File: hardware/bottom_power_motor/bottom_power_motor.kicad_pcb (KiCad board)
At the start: 4 copper layers, 52 x 52 mm, 82 parts, among them J1 Feld 16p, J2 J_STK_A, J3 J_STK_B, Q1 P-FET 40V 30A, U2 TPS54360, U2_CB 100n, U2_CO 47u, U2_CZ 3n3, U2_D 60V 3A, U2_L 10u, U2_RC 10k, U2_RH 53k6, U2_RL 10k2, U2_RT_R 100k, U3 TLV62569, U4 TPS54360, U4_CB 100n, U4_CO 22u, U4_CZ 3n3, U4_D 60V 3A, U4_L 33u, U4_RC 10k, U4_RH 68k1, U4_RL 10k0, U4_RT_R 100k

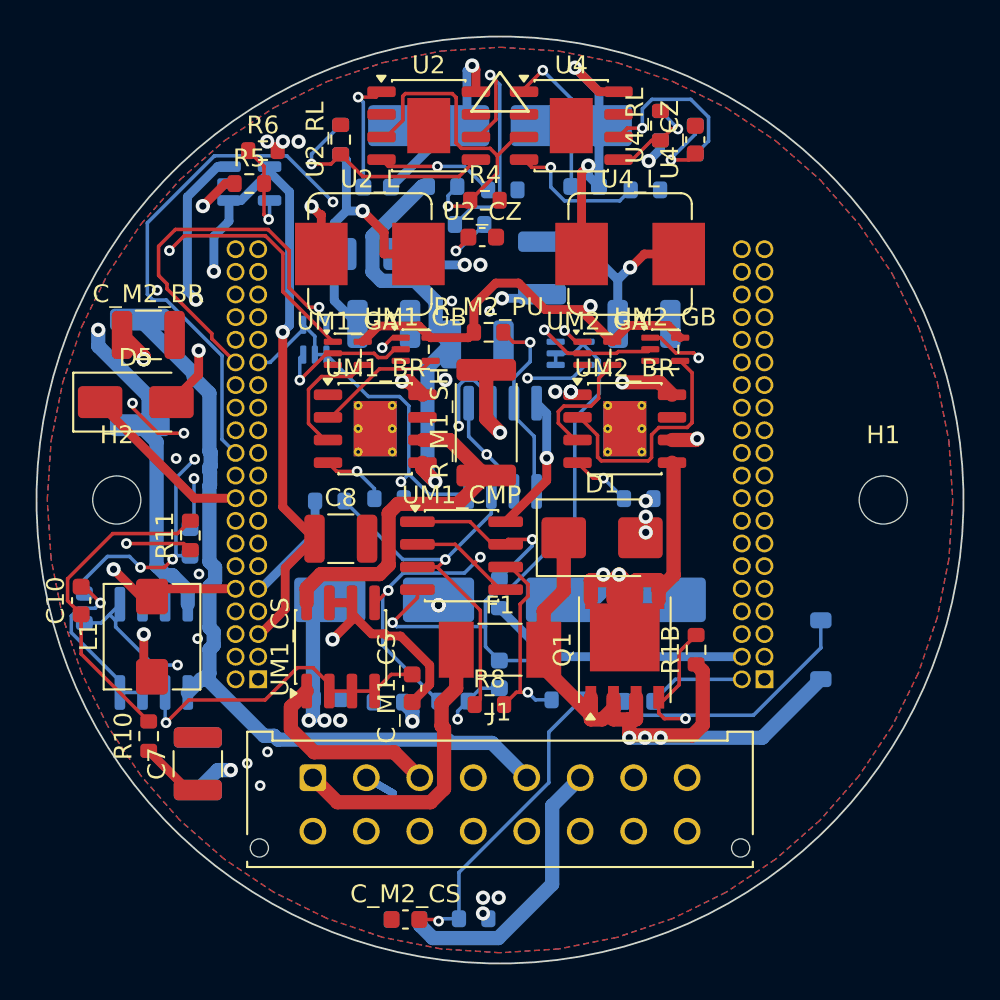
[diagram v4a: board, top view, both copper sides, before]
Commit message: Bestellfaehigkeit Punkt fuer Punkt - und das Flip-Flop war unbestueckbar
Die Frage "was ist entscheidend fuer Fertigung und Bestueckung?" wurde als
Sieben-Punkte-Liste beantwortet und abgearbeitet:

1. NETZE: Zweiter Freerouting-Pass ueber alle drei Boards - die neue
Erkenntnis (Altbahnen gelten als Vorverdrahtung) als Werkzeug genutzt.
Mid faellt auf 3 offene Signale. Top ist geometrisch festgefahren (9),
Bottom nach Neuerzeugung bei seinen Restnetzen - alles dokumentierte
Handarbeit in docs/16. gen_fab bleibt bis dahin zu Recht verriegelt.

2. KUPFER: Alle drei Boards null Fehler. Drei Nacharbeiten auf dem Weg:
ein Brueckenvia 0,33 mm vor der Bottom-Kante nach innen gerueckt, das
RELAY_CTL-Segment an der USB-Bohrung erneut entfernt (Freerouting legt es
in dieselbe Luecke - ein Keepout scheidet aus, weil die USB-Pads nur
1,0 mm neben den Loechern liegen; bleibt Handarbeit), und die
LCSC-Felder unsichtbar gestellt, die als sieben ungespiegelte C-Nummern
im Bestueckungsdruck der Rueckseite auftauchten.

3. LCSC: 13 Nummern verifiziert (jede von einer LCSC-Produktseite,
nichts geraten) und doppelt verdrahtet - in den Schaltplan-Generatoren
fuer kuenftige Neuerzeugungen, per neuem tools/lcsc_nachtragen.py auf
den fertig gerouteten Boards. Fehlend: 262 statt 302. Ehrlich offen:
TLV3702 (LCSC fuehrt nur die TLC-Variante, die am Gleichtaktbereich
scheitert), VL53L1X, Micro-Fit 43045-1612 (THT, zur Not von Hand).

DER WICHTIGSTE FUND STECKTE IM LCSC-ABGLEICH: Das Trip-Latch 74AUP1G74
stand im 5-Pin-SOT-353 - ein D-Flip-Flop hat ACHT Pins, 6/7/8 hingen in
der Luft. Jedes gefertigte Bottom waere Schrott gewesen. Jetzt VSSOP-8
(SN74AUP1G74DCUR, C140267), Bottom komplett neu erzeugt und geroutet -
974 Segmente, 121 Vias, mit SENSE-Abstandsklasse (300 um) fuer
M1_ISNS/M2_ISNS gegen die Trip-Schwellen.

4. NUTZEN: kupferfehlerfrei; die zwoelf verbleibenden DRC-Meldungen sind
EINE Sache (Mausbiss-Bohrungen des 12-Uhr-Stegs in der grosszuegigen
ESP32-Sperrflaeche - kein Kupfer, en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
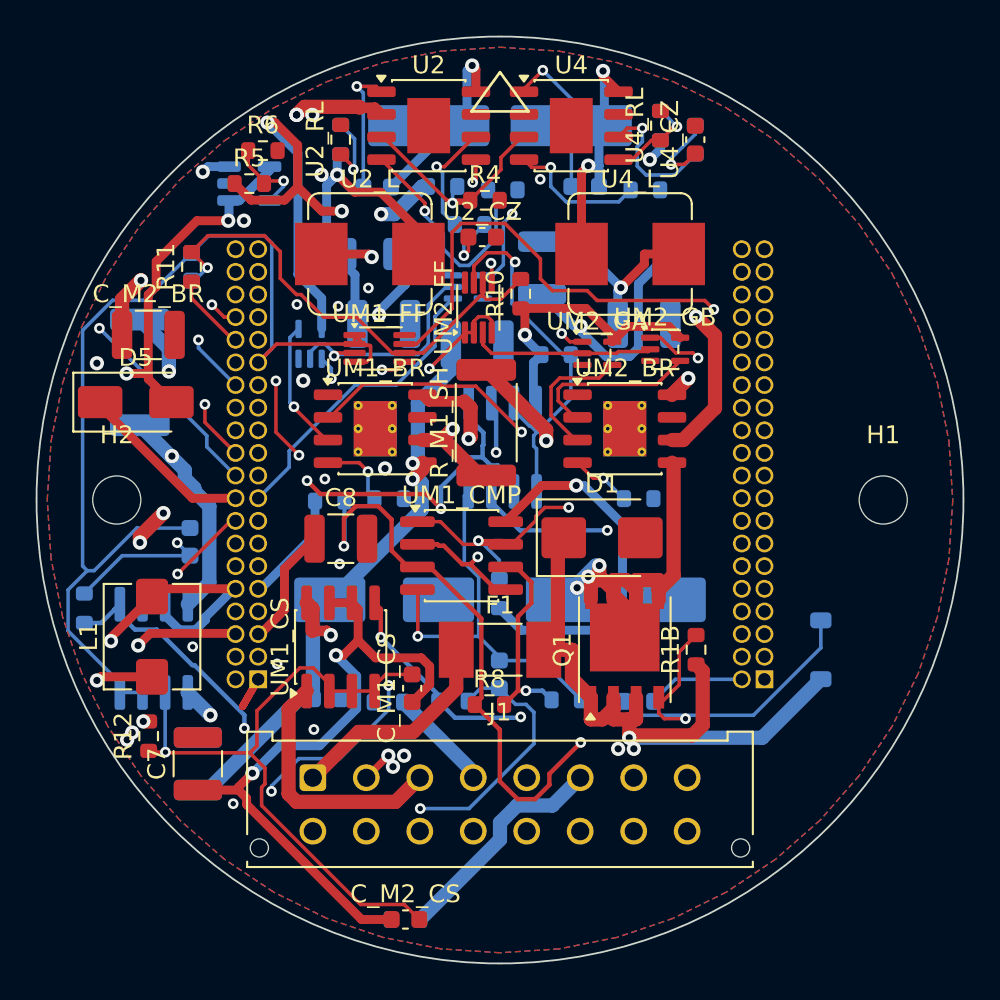
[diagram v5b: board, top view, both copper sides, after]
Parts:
- removed the UM1_FF at (-10.4, -8.99)
- removed the UM2_FF at (3.96, -8.23)
- added UM1_FF: 74AUP1G74, VSSOP-8_2.3x2mm_P0.5mm, F.Cu at (-6.76, -8.50)
- added UM2_FF: 74AUP1G74, VSSOP-8_2.3x2mm_P0.5mm, F.Cu at (-1.22, -10.8)
- C10, R_M2_PU, UM1_GA, UM1_GB: moved to B.Cu
- R12: moved to F.Cu
- moved R10 32.4 mm to (1.17, -11.6)
- moved R12 20.9 mm to (-19.7, 13.2), turned to 90 degrees
- moved C10 19.7 mm to (-17.3, -13.1)
- moved R11 15.1 mm to (-17.3, -13.1)
- moved UM1_GB 4.56 mm to (-1.80, -12.0)
- moved R_M2_PU 3.99 mm to (3.15, -8.15)
- moved UM1_GA 2.18 mm to (-10.7, -8.76), turned to 90 degrees
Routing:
- net M1_A: track 43.4 -> 97.3 mm
- net M1_TRIP: track 10.1 -> 55.2 mm, vias 1 -> 3
- net 3V3_SYS: track 160.4 -> 198.8 mm, vias 5 -> 7
- net V_TRIP_HI: track 22.5 -> 52.8 mm, vias 1 -> 3
- net M1_GB: track 7.07 -> 30.0 mm, vias 0 -> 2
- net TRIP_RST: track 22.7 -> 4.38 mm, vias 3 -> 0
- net M1_INA: track 31.0 -> 49.0 mm, vias 1 -> 4
- net 6V2_STAR_F: track 23.8 -> 41.2 mm, vias 1 -> 2
- net SAB1_IN: track 35.1 -> 50.7 mm, vias 0 -> 1
- net AGND: track 151.6 -> 137.6 mm, vias 6 -> 3
- net M2_INA: track 40.6 -> 53.1 mm
- net I_SENSE1: track 36.5 -> 47.7 mm, vias 3 -> 1
- net M2_ISNS: track 40.2 -> 50.8 mm, vias 2 -> 5
- net M2_TRIP: track 11.0 -> 21.5 mm
- net TRIP_CLR: track 18.1 -> 27.5 mm, vias 0 -> 1
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
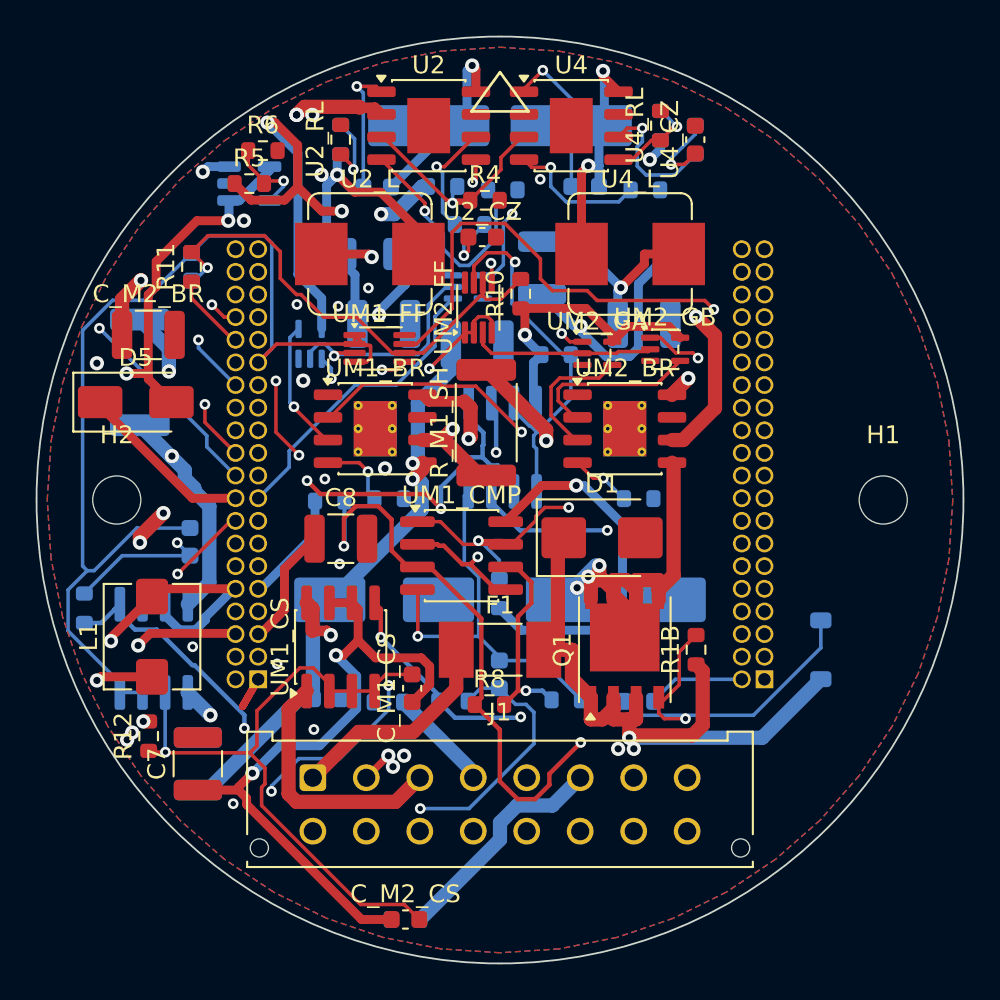
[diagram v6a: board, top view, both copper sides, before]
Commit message: Neue Ecktaster: Alps SKQG statt des abgekuendigten SKRK - in drei Anlaeufen
Der Ersatz fuer das abgekuendigte SKRKAEE010 (Punkt 69) ist der Alps
SKQGABE010, LCSC C115351: Original-Alps, 24.000 ab Lager, gleiche
Betaetigungskraft 1,6 N, und mit 5,2 x 5,2 die deutlich groessere Flaeche
unter dem Druckkreuz. Bauhoehe 1,5 statt 2,0 - switch_h in adapter.py
umgestellt, die Tiefenkette rechnet sich selbst neu (Platine 0,5 nach
vorn, Adapter im Stapel auf z 15,0, stack.py nachgezogen).

DIE POSITION BRAUCHTE DREI ANLAEUFE, jeder DRC-belegt:
  18,0/20,0  - aeussere Padecke 0,17 mm vor dem Eckbogen (4 Randfehler)
  17,7/19,7  - der 8,6 mm breite Courtyard ueberlappte den Hauptschalter
               SW5, und zwei Masse-Brueckenvias sassen in der
               Via-Sperrflaeche unter dem Tasterdom
  18,1/19,35 - passt: 0,56 zum Bogen, 0,2 zu SW5, Druckkreuz behaelt
               0,35 Deckungsreserve auf der Tasterflaeche

gnd_connect meidet seither Footprint-Sperrflaechen (GetDoNotAllowVias) -
der SKQG verbietet Vias unter seinem Metalldom, und das Werkzeug setzte
prompt zwei hinein.

BILANZ DER GESAMTEN LCSC-RUNDE (drei Ketten): Im Nutzen fehlen noch 30
von 131 Positionen - ausschliesslich Portal-Parameterwahl (E96-Werte,
1210-Kondensatoren, Zener-Rest, Stapelverbinder, offene FET-Typen).
Alle drei Boards null Kupferfehler:
  Top     160 Seg,  19 Vias (SKQG-Taster, alle Nummern gesetzt)
  Mid     776 Seg,  85 Vias
  Bottom 1103 Seg, 129 Vias (Polymer-Bulk, Sicherung flink, FF VSSOP-8)

Co-Authored-By: Claude Opus 5 <noreply@anthropic.com>
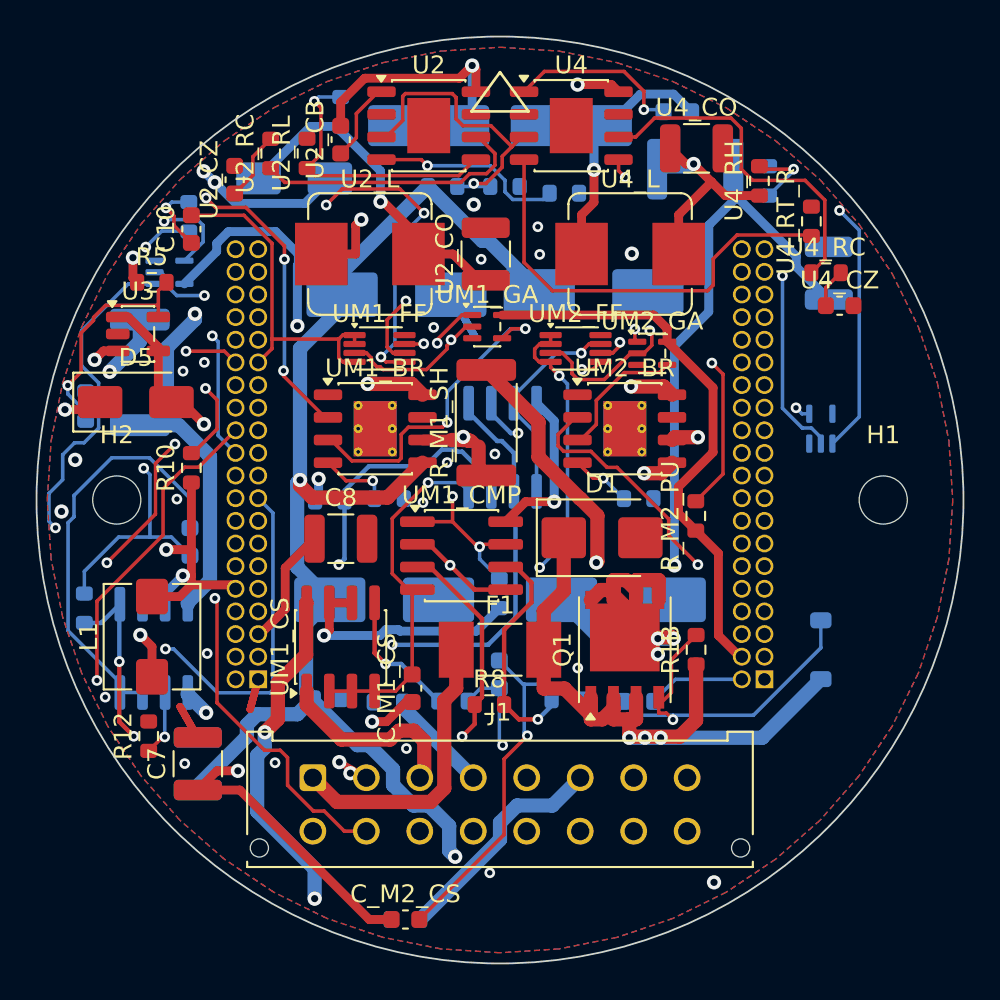
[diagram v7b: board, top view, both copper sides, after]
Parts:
- removed the C_M1_BR at (-1.28, -8.73)
- removed the C_M2_BR at (-19.7, -9.26)
- added C_M1_BR: 100u/35V Polymer, CP_Elec_8x6.5, B.Cu at (-5.81, -11.5)
- added C_M2_BR: 100u/35V Polymer, CP_Elec_8x6.5, B.Cu at (5.25, -11.7)
- C10, R_M2_PU, U2_CB, U2_CO, U2_RC, U3, U4_CO, U4_RC, U4_RH, U4_RT_R, UM1_GA: moved to F.Cu
- F1: value 15A traege -> 15A flink
- R11, R4, R6, U4_RL, UM2_GB: moved to B.Cu
- moved R10 20.9 mm to (-17.3, -1.80)
- moved R6 17.4 mm to (-23.2, -5.27), turned to 90 degrees
- moved UM1_GB 16.8 mm to (-18.5, -12.8)
- moved C9 16.1 mm to (18.4, -12.7)
- moved U2_CZ 14.3 mm to (-14.9, -18.0), turned to 90 degrees
- moved U4_CZ 12.3 mm to (19.1, -10.9), turned to 0 degrees
- moved R_M2_PU 12.0 mm to (11.0, 0.90), turned to 90 degrees
- moved U2_RC 11.8 mm to (-12.9, -19.4), turned to 90 degrees
- moved U3 10.5 mm to (-20.3, -9.31)
- moved U4_RC 10.5 mm to (18.3, -12.8), turned to 0 degrees
- moved U4_CO 10.3 mm to (11.0, -19.7)
- moved UM1_GA 9.98 mm to (-0.72, -9.73), turned to 0 degrees
- moved UM2_GB 9.80 mm to (18.0, -4.00), turned to 90 degrees
- moved U4_RT_R 9.48 mm to (17.5, -15.6), turned to 90 degrees
- moved R5 7.78 mm to (-19.5, -12.2)
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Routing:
- net M1_SWA: track 26.3 -> 109.7 mm, vias 3 -> 5
- net M1_A: track 97.3 -> 40.4 mm
- net TRIP_CLR: track 27.5 -> 67.5 mm, vias 1 -> 5
- net M1_TRIP: track 55.2 -> 21.6 mm, vias 3 -> 4
- net M2_GB: track 9.63 -> 40.9 mm, vias 0 -> 2
- net M1_INB: track 17.1 -> 46.8 mm, vias 0 -> 2
- net M1_INA: track 49.0 -> 76.6 mm, vias 4 -> 3
- net M1_SD: track 13.0 -> 37.7 mm, vias 1 -> 3
- net AGND: track 137.6 -> 161.1 mm, vias 3 -> 5
- net 6V2_STAR_F: track 41.2 -> 61.9 mm, vias 2 -> 1
- net M2_SD: track 10.4 -> 30.8 mm, vias 0 -> 2
- net PGND: track 8.75 -> 27.8 mm, vias 6 -> 3
- net M2_INA: track 53.1 -> 70.8 mm
- net U4_RT: track 7.87 -> 24.7 mm, vias 1 -> 0
- net SAB1_IN: track 50.7 -> 35.4 mm, vias 1 -> 0
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
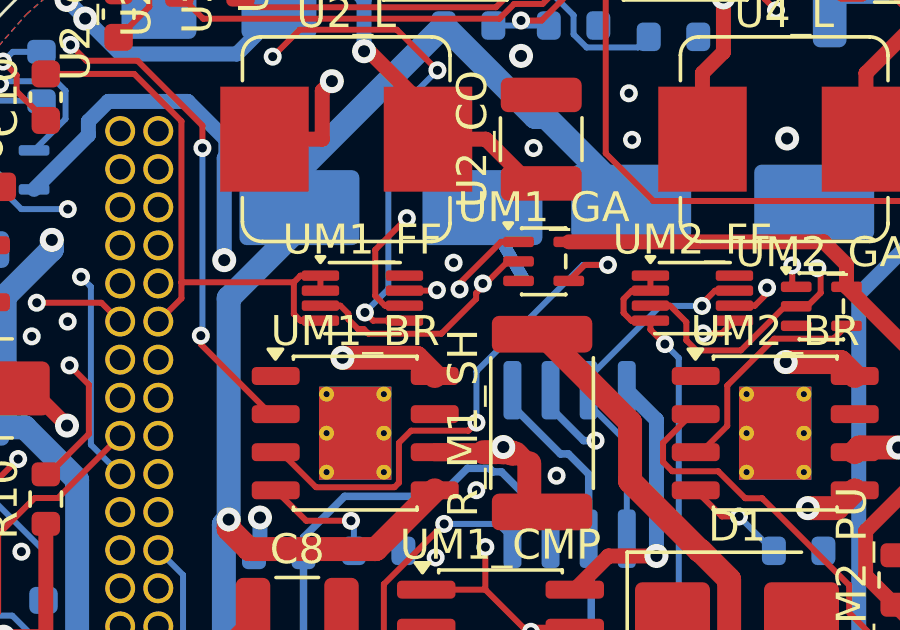
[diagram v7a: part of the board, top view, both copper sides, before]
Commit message: Der Rest-Schliesser findet seine Netze - drei Reparaturen und ein ehrliches Ende
Die Kette pass3 + rest_schliessen lief scheinbar durch, hatte aber drei
Loecher: GetBoardPolygonOutlines braucht in KiCad 10 ein zweites
Argument (beide Runden crashten sofort), Outline(0) liefert eine
SWIG-Referenz ins freigegebene Poly-Set (Segfault ohne Traceback, per
faulthandler gefunden), und KiCad 10 schreibt den Netznamen nicht als
Feld ins DRC-JSON, sondern nur in den Beschreibungstext - beide
Werkzeuge lasen also fuer jede offene Verbindung ein leeres Netz.
Dazu ein neuer Fall: deckungsgleiche Pads auf F und B bekommen ein
Via mittenhinein.

Freerouting hatte im pass3 ausserdem RELAY_CTL wieder 15 um zu nah an
der USB-NPTH vorbeigelegt - zwei Segmente raus, wie beim letzten Mal.

Endstand nach drei Runden: Top 4, Mid 15, Bottom 28 offene
Verbindungen, alle Boards 0 Kupferfehler. Mehr schliesst das Werkzeug
nicht - die Restfaelle brauchen Via-Umwege, das ist die dokumentierte
Handarbeit. docs/16: Engpassliste auf den neuen Stand (die Stellen
sind mit dem Neurouting gewandert), die laengst ausgebaute
Klinkenbuchse aus dem Masse-Kapitel entfernt.

Co-Authored-By: Claude Opus 5 <noreply@anthropic.com>
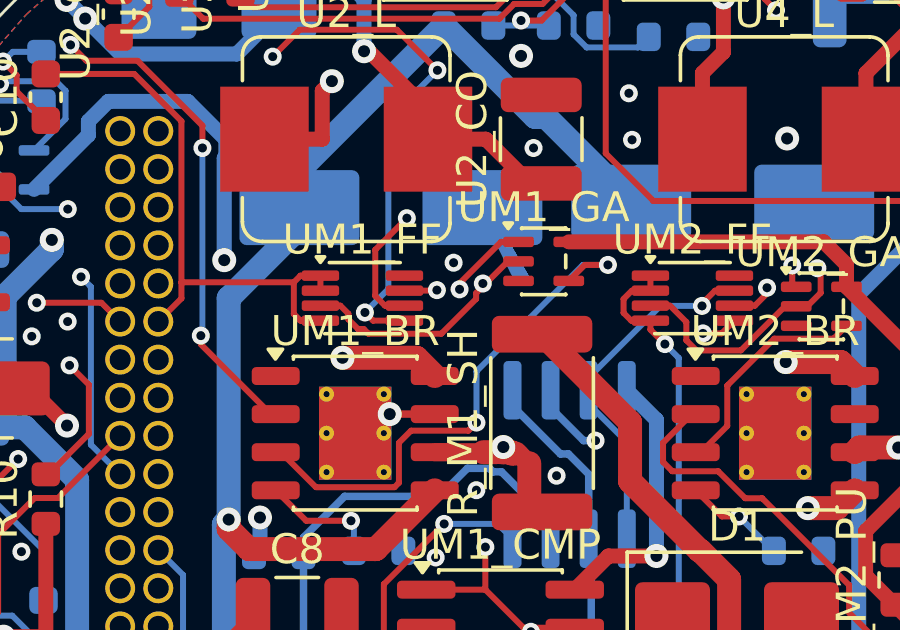
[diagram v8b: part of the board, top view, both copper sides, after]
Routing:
- net PGND: track 27.8 -> 32.0 mm, vias 3 -> 4
